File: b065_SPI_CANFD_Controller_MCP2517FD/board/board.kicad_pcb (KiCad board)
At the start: 2 copper layers, 21 x 13 mm, 9 parts, among them J1 002_SPI, J2 012_CAN, U1 MCP2517FD-xSL, Y1 20MhZ

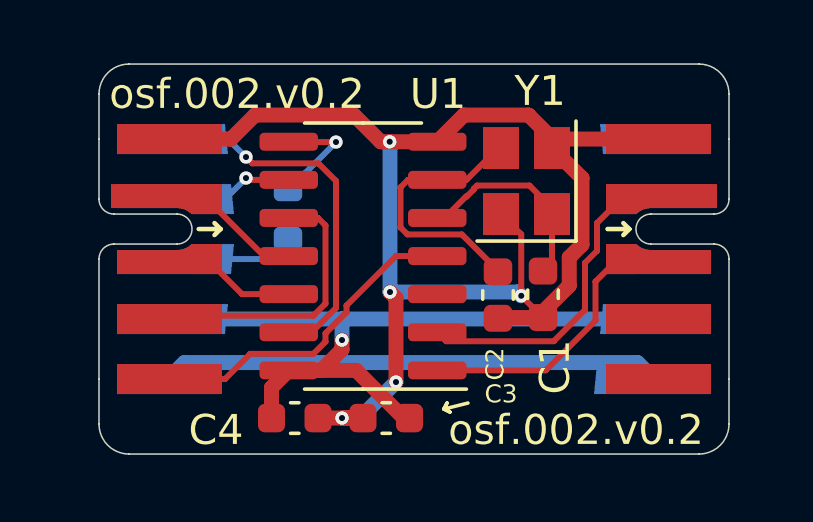
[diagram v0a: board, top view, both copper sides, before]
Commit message: updated to kicad 6
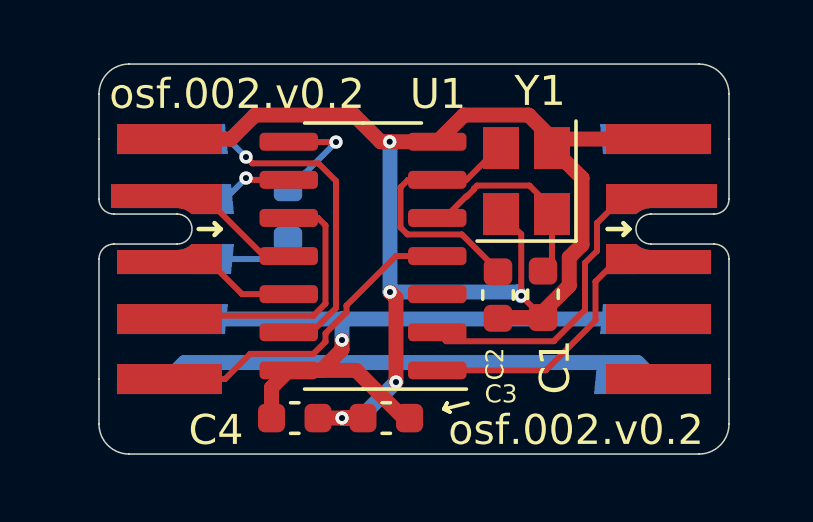
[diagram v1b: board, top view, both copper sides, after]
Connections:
- J2 pad 5: (no net) -> unconnected-(J2-Pad5)
- J2 pad 6: (no net) -> unconnected-(J2-Pad6)
- J2 pad 7: (no net) -> unconnected-(J2-Pad7)
- J2 pad 8: (no net) -> unconnected-(J2-Pad8)
- U1 pad 3: (no net) -> unconnected-(U1-Pad3)
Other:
- net class Default removed

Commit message: updated quarz to 40mhz
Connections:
- J2 pad 5: unconnected-(J2-Pad5) -> (no net)
- J2 pad 6: unconnected-(J2-Pad6) -> (no net)
- J2 pad 7: unconnected-(J2-Pad7) -> (no net)
- J2 pad 8: unconnected-(J2-Pad8) -> (no net)
- U1 pad 3: unconnected-(U1-Pad3) -> (no net)
